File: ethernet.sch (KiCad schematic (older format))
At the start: 41 parts, among them J201 SI-52008-F, U201 ENC28J60x-SS, U202 TPS54231, Y201 Crystal

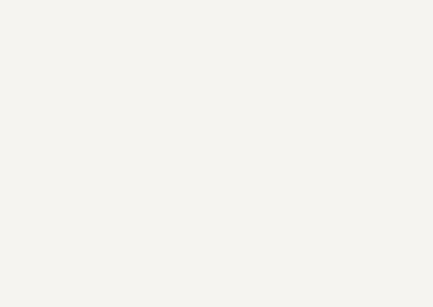
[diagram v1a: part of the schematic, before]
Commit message: Platzierung begonnen, Signalnamen ENC korrigiert
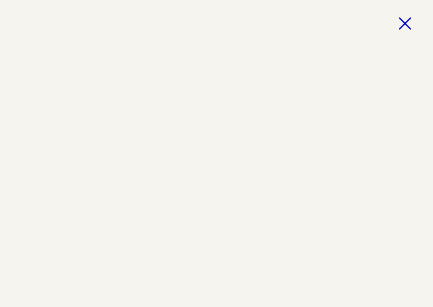
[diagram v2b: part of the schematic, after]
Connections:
- no-connect marks 4 -> 5
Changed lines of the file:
@@
 Wire Wire Line
 	9200 2700 9200 2550
+NoConn ~ 10950 -500
 $EndSCHEMATC

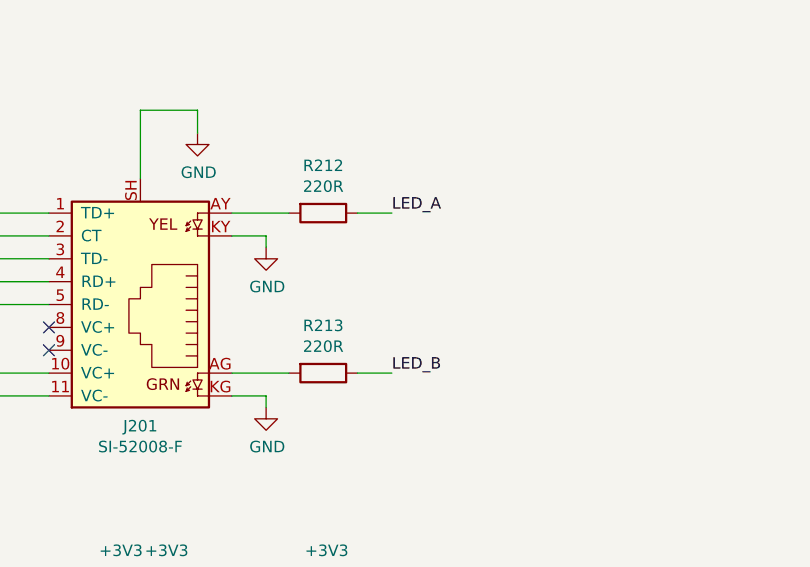
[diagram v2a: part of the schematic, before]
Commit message: ENC28J60 platziert und geroutet
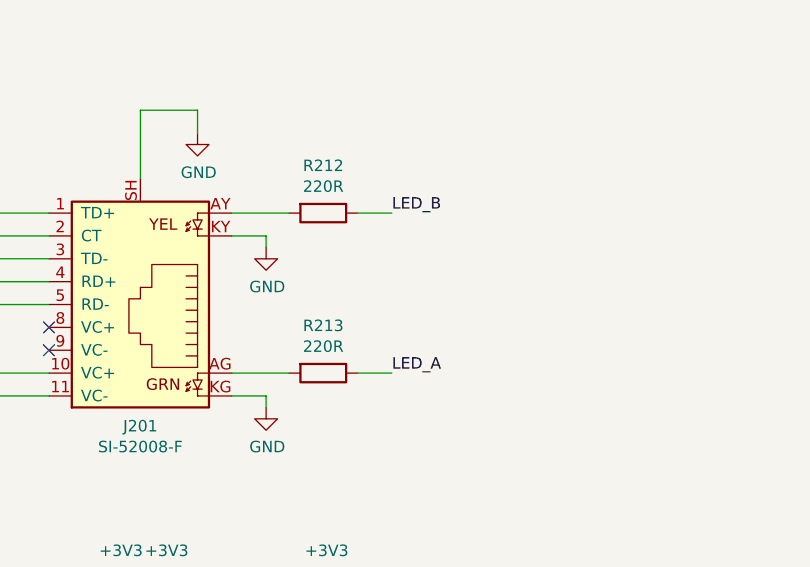
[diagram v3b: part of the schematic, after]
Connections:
- net LED_A: now also R213.1; no longer R212.1
- net LED_B: now also R212.1; no longer R213.1
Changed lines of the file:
@@
 Wire Wire Line
 	4250 2100 4100 2100
+Text Label 4800 2700 0    50   ~ 0
+LED_A
 Text Label 4800 2000 0    50   ~ 0
-LED_A
-Text Label 4800 2700 0    50   ~ 0
 LED_B
-Wire Wire Line
-	4800 2700 4650 2700
-Wire Wire Line
-	4800 2000 4650 2000
 NoConn ~ 3300 2500
 NoConn ~ 3300 2600
@@
 	9200 2700 9200 2550
 NoConn ~ 10950 -500
+Wire Wire Line
+	4800 2000 4650 2000
+Wire Wire Line
+	4650 2700 4800 2700
 $EndSCHEMATC

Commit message: Design weiter bearbeitet
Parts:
- removed C207, C213, C215: 10U, Capacitor_SMD:C_1210_3225Metric, symbol Device:C
- removed C214: 47U, Capacitor_SMD:C_1210_3225Metric, symbol Device:C
- added C207: 10U, symbol Device:CP
- added C213, C215: 10U, Capacitor_SMD:CP_Elec_5x5.4, symbol Device:CP
- added C214: 47U, Capacitor_SMD:CP_Elec_6.3x7.7, symbol Device:CP
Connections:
- net +24V: now also C213.1, C215.1
- net GND: now also C207.2, C213.2, C214.2, C215.2
- net at U201.1 (VCAP): now also C207.1
- net at L201.2, R218.2: now also C214.1
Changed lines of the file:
@@
-$EndComp
-$Comp
-L Device:C C207
-U 1 1 5C096F4C
-P 4850 6350
-F 0 "C207" H 4965 6396 50  0000 L CNN
-F 1 "10U" H 4965 6305 50  0000 L CNN
-F 2 "Capacitor_SMD:C_1210_3225Metric" H 4888 6200 50  0001 C CNN
-F 3 "~" H 4850 6350 50  0001 C CNN
-	1    4850 6350
-	1    0    0    -1
 $EndComp
 $Comp
@@
 $EndComp
 $Comp
-L Device:C C213
-U 1 1 5C174089
-P 9550 2950
-F 0 "C213" H 9665 2996 50  0000 L CNN
-F 1 "10U" H 9665 2905 50  0000 L CNN
-F 2 "Capacitor_SMD:C_1210_3225Metric" H 9588 2800 50  0001 C CNN
-F 3 "~" H 9550 2950 50  0001 C CNN
-	1    9550 2950
-	1    0    0    -1
-$EndComp
-$Comp
 L Device:C C212
 U 1 1 5C174238
@@
 Wire Wire Line
 	9600 3800 9700 3800
-$Comp
-L Device:C C214
-U 1 1 5C184DCA
-P 10250 4050
-F 0 "C214" H 10135 4004 50  0000 R CNN
-F 1 "47U" H 10135 4095 50  0000 R CNN
-F 2 "Capacitor_SMD:C_1210_3225Metric" H 10288 3900 50  0001 C CNN
-F 3 "~" H 10250 4050 50  0001 C CNN
-	1    10250 4050
-	-1   0    0    1
-$EndComp
 Wire Wire Line
 	10000 3800 10250 3800
@@
 ENC_#INT
 $Comp
-L Device:C C215
-U 1 1 5C2986FF
-P 10050 2950
-F 0 "C215" H 10165 2996 50  0000 L CNN
-F 1 "10U" H 10165 2905 50  0000 L CNN
-F 2 "Capacitor_SMD:C_1210_3225Metric" H 10088 2800 50  0001 C CNN
-F 3 "~" H 10050 2950 50  0001 C CNN
-	1    10050 2950
-	1    0    0    -1
-$EndComp
-$Comp
 L power:GND #PWR0236
 U 1 1 5C298767
@@
 Wire Wire Line
 	4650 2700 4800 2700
+$Comp
+L Device:CP C215
+U 1 1 5C0DA45D
+P 10050 2950
+F 0 "C215" H 10168 2996 50  0000 L CNN
+F 1 "10U" H 10168 2905 50  0000 L CNN
+F 2 "Capacitor_SMD:CP_Elec_5x5.4" H 10088 2800 50  0001 C CNN
+F 3 "~" H 10050 2950 50  0001 C CNN
+	1    10050 2950
+	1    0    0    -1
+$EndComp
+$Comp
+L Device:CP C213
+U 1 1 5C0EDFF6
+P 9550 2950
+F 0 "C213" H 9668 2996 50  0000 L CNN
+F 1 "10U" H 9668 2905 50  0000 L CNN
+F 2 "Capacitor_SMD:CP_Elec_5x5.4" H 9588 2800 50  0001 C CNN
+F 3 "~" H 9550 2950 50  0001 C CNN
+	1    9550 2950
+	1    0    0    -1
+$EndComp
+$Comp
+L Device:CP C214
+U 1 1 5C0FD1EE
+P 10250 4050
+F 0 "C214" H 10368 4096 50  0000 L CNN
+F 1 "47U" H 10368 4005 50  0000 L CNN
+F 2 "Capacitor_SMD:CP_Elec_6.3x7.7" H 10288 3900 50  0001 C CNN
+F 3 "~" H 10250 4050 50  0001 C CNN
+	1    10250 4050
+	1    0    0    -1
+$EndComp
+$Comp
+L Device:CP C207
+U 1 1 5C10C874
+P 4850 6350
+F 0 "C207" H 4968 6396 50  0000 L CNN
+F 1 "10U" H 4968 6305 50  0000 L CNN
+F 2 "" H 4888 6200 50  0001 C CNN
+F 3 "~" H 4850 6350 50  0001 C CNN
+	1    4850 6350
+	1    0    0    -1
+$EndComp
 $EndSCHEMATC

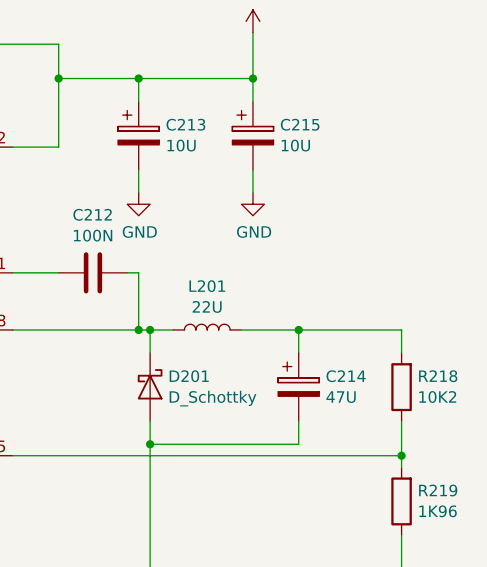
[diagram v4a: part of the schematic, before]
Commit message: TPS54231 geroutet
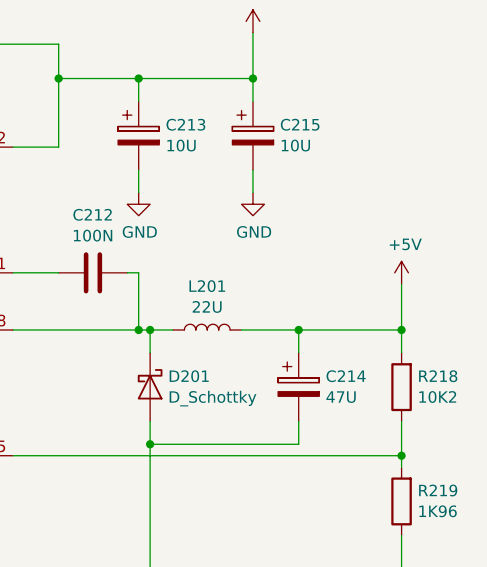
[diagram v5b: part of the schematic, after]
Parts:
- C207: footprint (none) -> Capacitor_Tantalum_SMD:CP_EIA-6032-28_Kemet-C
- C214: footprint Capacitor_SMD:CP_Elec_6.3x7.7 -> Capacitor_Tantalum_SMD:CP_EIA-6032-28_Kemet-C
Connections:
- net +5V: now reaches C214.1, L201.2, R218.2
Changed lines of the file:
@@
 F 0 "C214" H 10368 4096 50  0000 L CNN
 F 1 "47U" H 10368 4005 50  0000 L CNN
-F 2 "Capacitor_SMD:CP_Elec_6.3x7.7" H 10288 3900 50  0001 C CNN
+F 2 "Capacitor_Tantalum_SMD:CP_EIA-6032-28_Kemet-C" H 10288 3900 50  0001 C CNN
 F 3 "~" H 10250 4050 50  0001 C CNN
 	1    10250 4050
@@
 F 0 "C207" H 4968 6396 50  0000 L CNN
 F 1 "10U" H 4968 6305 50  0000 L CNN
-F 2 "" H 4888 6200 50  0001 C CNN
+F 2 "Capacitor_Tantalum_SMD:CP_EIA-6032-28_Kemet-C" H 4888 6200 50  0001 C CNN
 F 3 "~" H 4850 6350 50  0001 C CNN
 	1    4850 6350
 	1    0    0    -1
 $EndComp
+$Comp
+L power:+5V #PWR?
+U 1 1 5C0FB918
+P 10700 3600
+F 0 "#PWR?" H 10700 3450 50  0001 C CNN
+F 1 "+5V" H 10715 3773 50  0000 C CNN
+F 2 "" H 10700 3600 50  0001 C CNN
+F 3 "" H 10700 3600 50  0001 C CNN
+	1    10700 3600
+	1    0    0    -1
+$EndComp
+Wire Wire Line
+	10700 3600 10700 3800
+Connection ~ 10700 3800
 $EndSCHEMATC

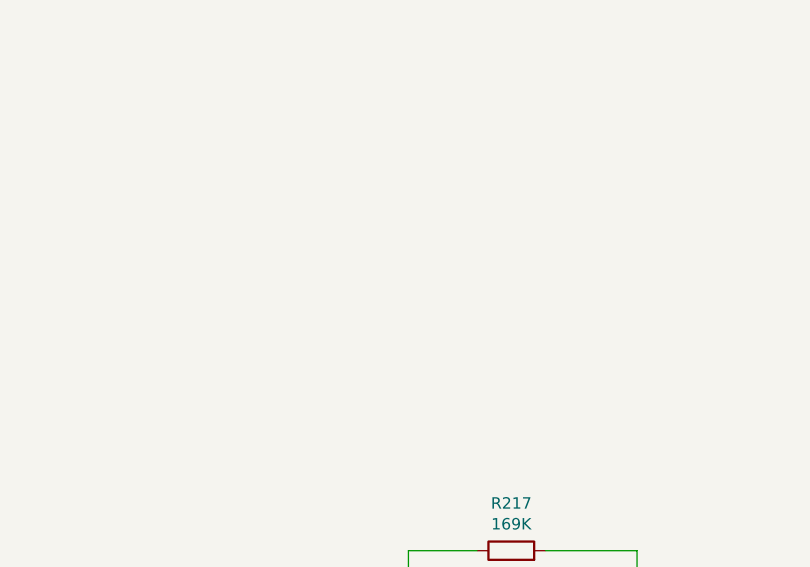
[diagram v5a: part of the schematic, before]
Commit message: Transistoren für Relais eingefügt, Pull-Ups für I2C, zusätzlicher Spannungseingang, Layout fertig
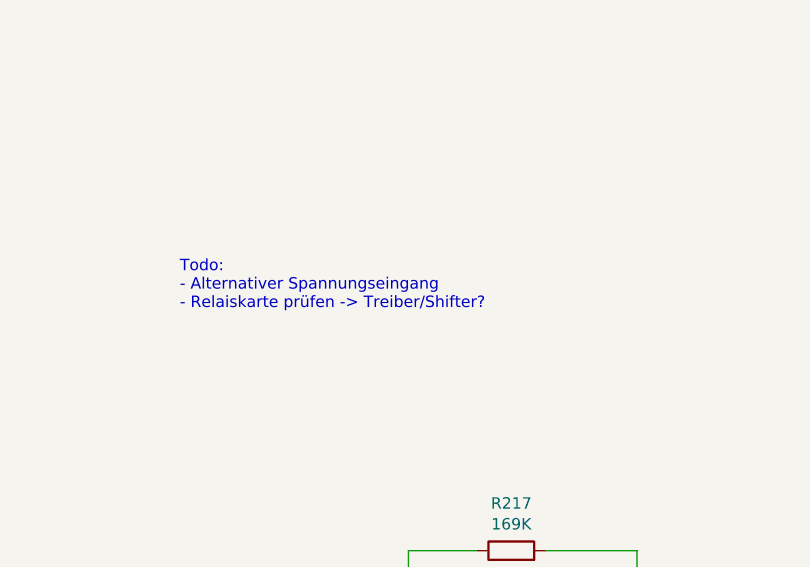
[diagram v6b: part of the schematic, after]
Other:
- note added: "Todo:\n- Alternativer Spannungseingang\n- Relaiskarte prüfen -> Treiber/Shifter?"
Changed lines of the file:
@@
 $Descr A4 11693 8268
 encoding utf-8
-Sheet 2 3
+Sheet 2 4
 Title ""
 Date ""
@@
 $EndComp
 $Comp
-L power:+5V #PWR?
+L power:+5V #PWR0115
 U 1 1 5C0FB918
 P 10700 3600
-F 0 "#PWR?" H 10700 3450 50  0001 C CNN
+F 0 "#PWR0115" H 10700 3450 50  0001 C CNN
 F 1 "+5V" H 10715 3773 50  0000 C CNN
 F 2 "" H 10700 3600 50  0001 C CNN
@@
 	10700 3600 10700 3800
 Connection ~ 10700 3800
+Text Notes 7200 1500 0    50   ~ 0
+Todo:\n- Alternativer Spannungseingang\n- Relaiskarte prüfen -> Treiber/Shifter?
 $EndSCHEMATC

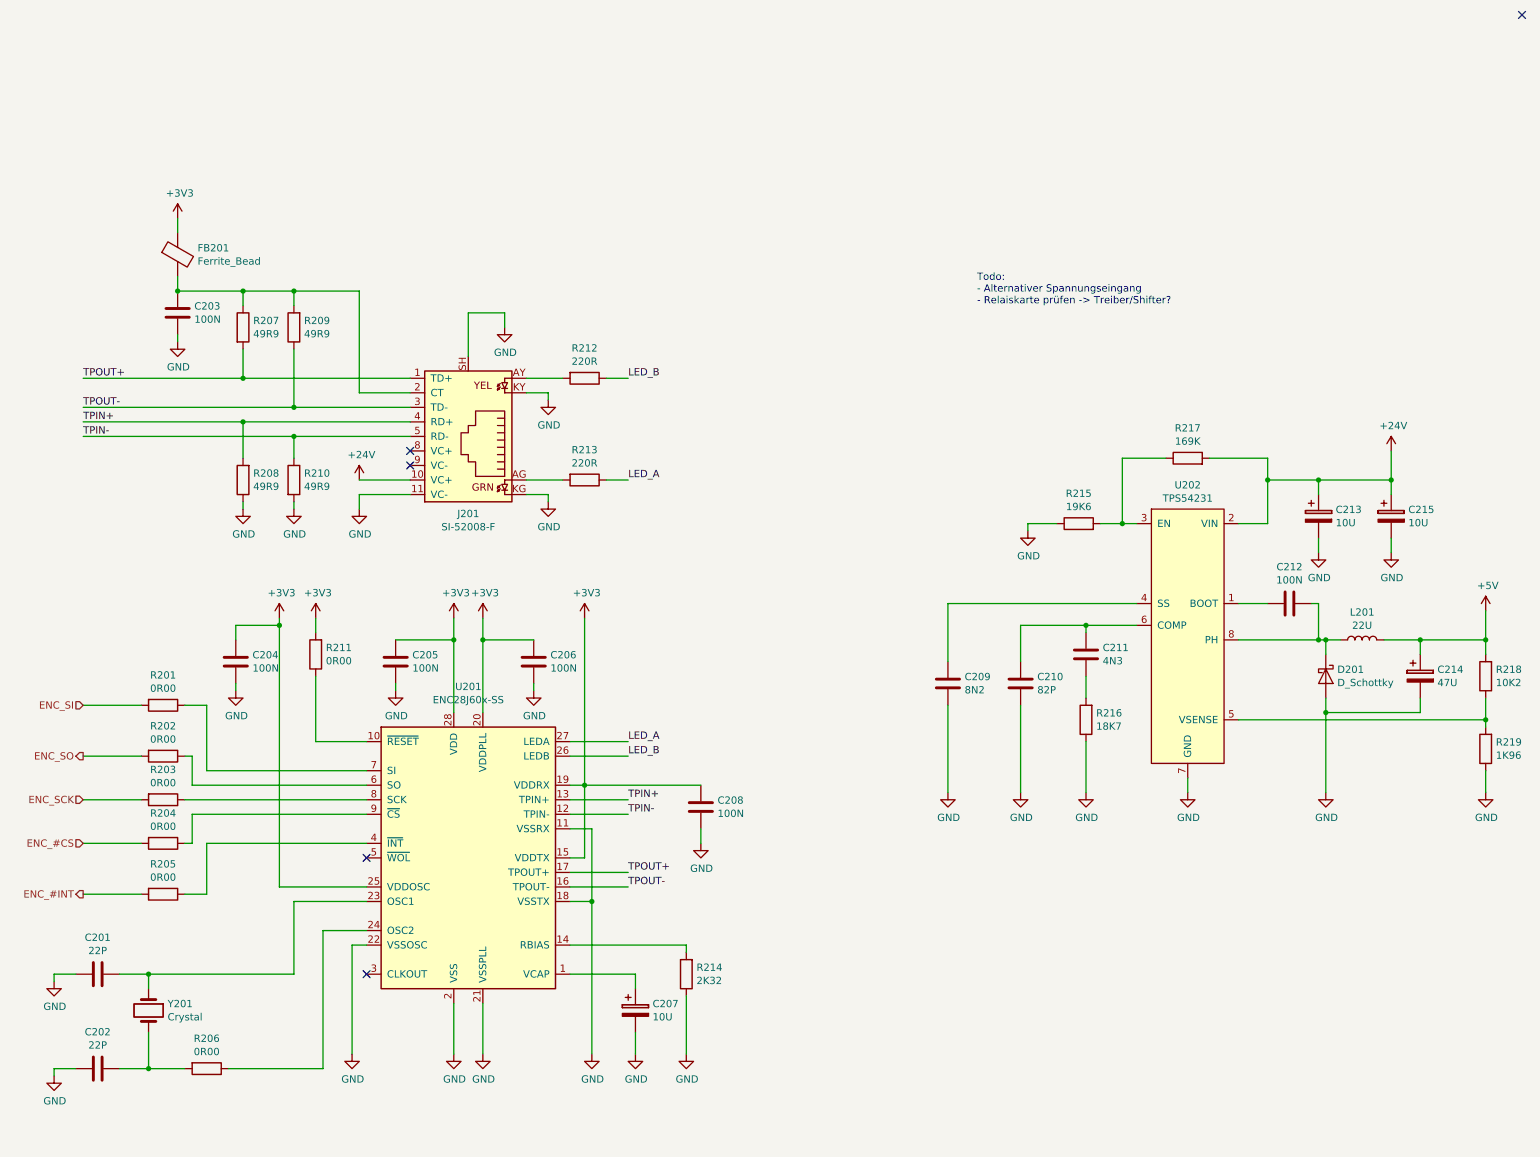
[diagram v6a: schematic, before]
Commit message: Änderungen nach Review, Layout fertig
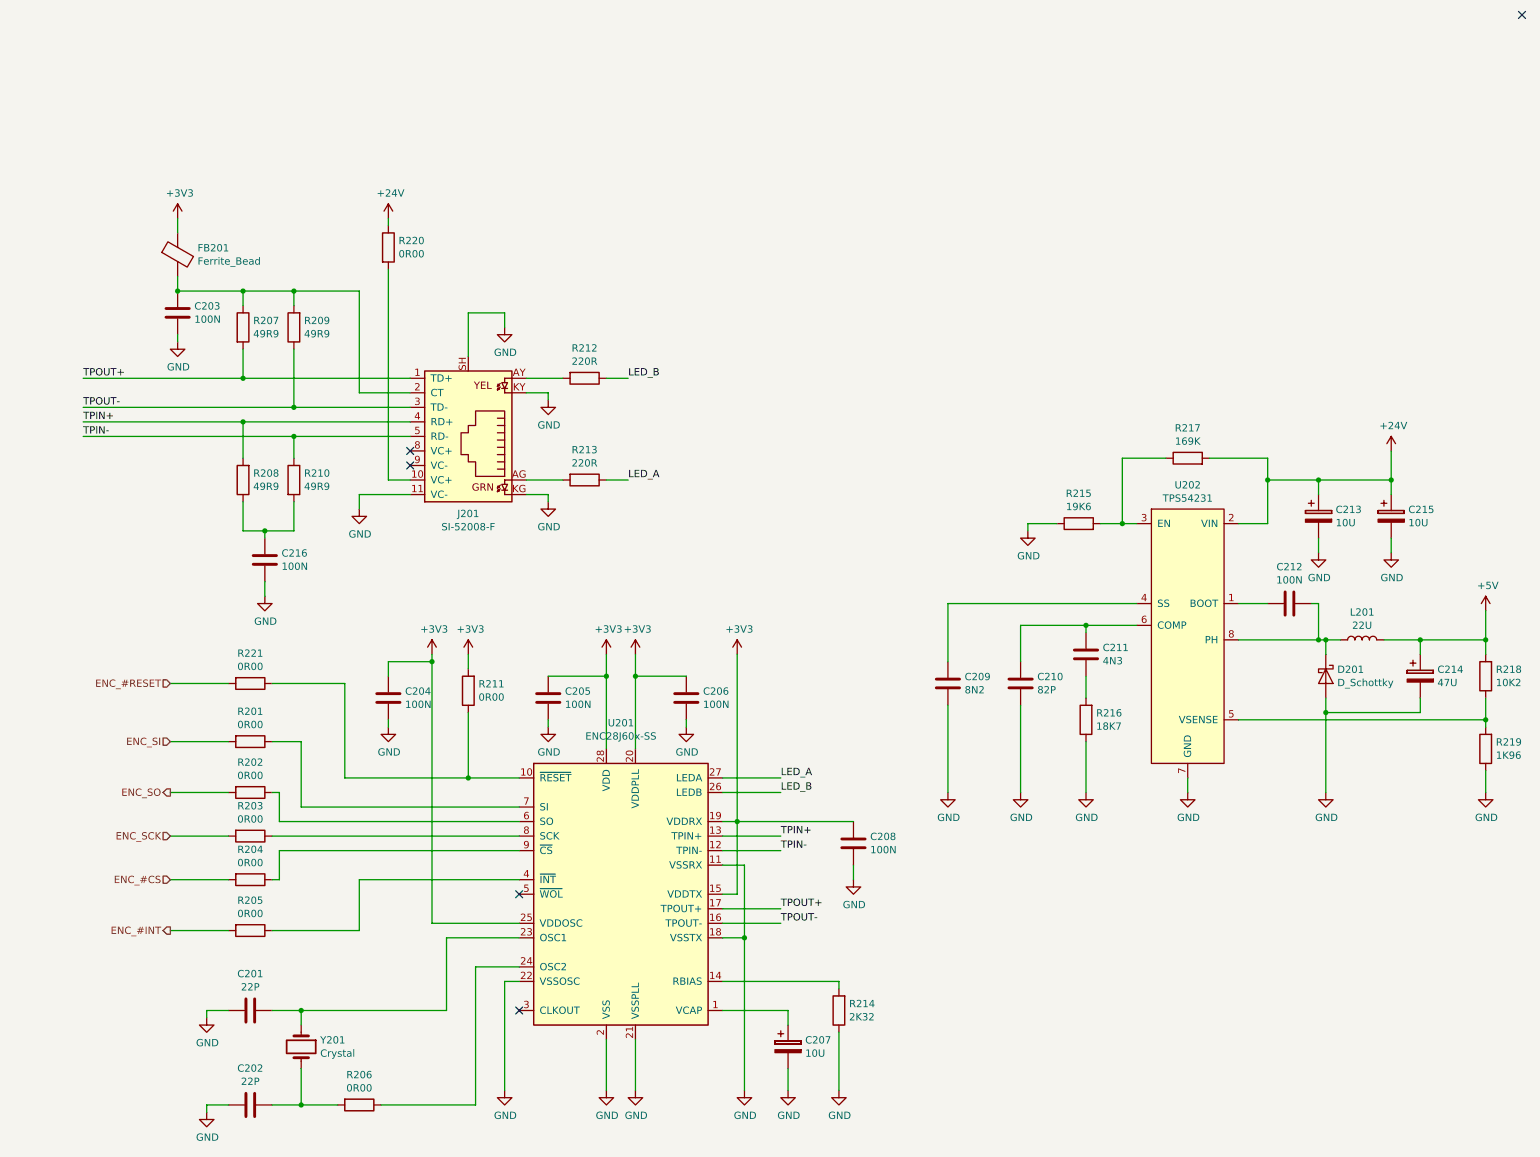
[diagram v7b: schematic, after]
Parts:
- added C216: 100N, Capacitor_SMD:C_0603_1608Metric, symbol Device:C
- added R220: 0R00, Resistor_SMD:R_1206_3216Metric, symbol Device:R
- added R221: 0R00, Resistor_SMD:R_0603_1608Metric, symbol Device:R
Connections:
- net +24V: now also R220.1; no longer J201.10 (VC+)
- net GND: now also C216.2; no longer R208.1, R210.2
- net at R211.1, U201.10 (~RESET): now also R221.1
- new net: J201.10 (VC+), R220.2
- new net: C216.1, R208.1, R210.2
- new net ENC_#RESET: R221.2
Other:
- note removed: "Todo:\n- Alternativer Spannungseingang\n- Relaiskarte prüfen -> Treiber/Shifter?"
- moved on the sheet: C201, C202, C204, C205, C206, C207, C208, R201, R202, R203, R204, R205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

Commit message: Bauteilwerte beim Bestücken angepasst
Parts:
- C211: value 4N3 -> 4N7
- R218: value 10K2 -> 12k0
- R219: value 1K96 -> 2k2
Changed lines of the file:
@@
 P 10700 4550
 F 0 "R219" H 10630 4504 50  0000 R CNN
-F 1 "1K96" H 10630 4595 50  0000 R CNN
+F 1 "2k2" H 10630 4595 50  0000 R CNN
 F 2 "Resistor_SMD:R_0603_1608Metric" V 10630 4550 50  0001 C CNN
 F 3 "~" H 10700 4550 50  0001 C CNN
@@
 P 10700 4050
 F 0 "R218" H 10630 4004 50  0000 R CNN
-F 1 "10K2" H 10630 4095 50  0000 R CNN
+F 1 "12k0" H 10630 4095 50  0000 R CNN
 F 2 "Resistor_SMD:R_0603_1608Metric" V 10630 4050 50  0001 C CNN
 F 3 "~" H 10700 4050 50  0001 C CNN
@@
 P 7950 3900
 F 0 "C211" H 7835 3854 50  0000 R CNN
-F 1 "4N3" H 7835 3945 50  0000 R CNN
+F 1 "4N7" H 7835 3945 50  0000 R CNN
 F 2 "Capacitor_SMD:C_0603_1608Metric" H 7988 3750 50  0001 C CNN
 F 3 "~" H 7950 3900 50  0001 C CNN
